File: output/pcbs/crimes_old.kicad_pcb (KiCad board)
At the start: 2 copper layers, 274.5 x 98.9 mm, 156 parts

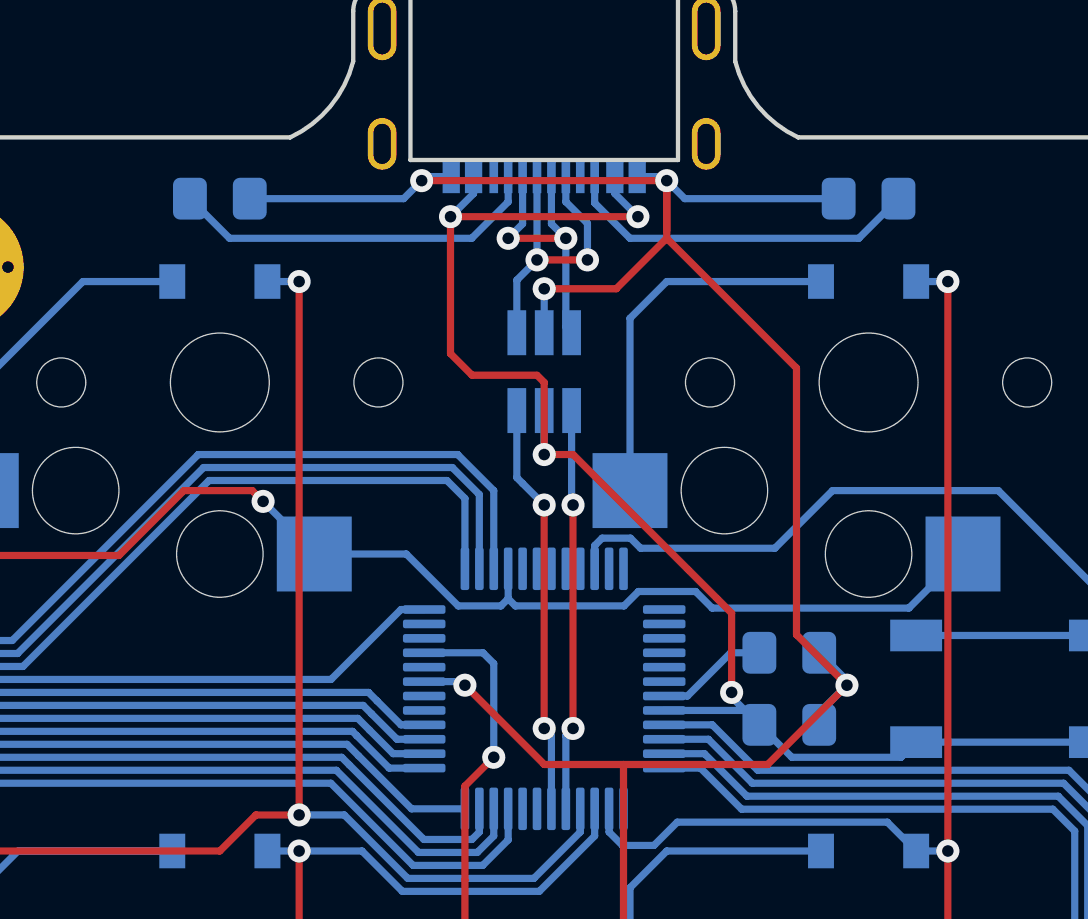
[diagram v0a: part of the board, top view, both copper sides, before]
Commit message: Fixed Pinouts.
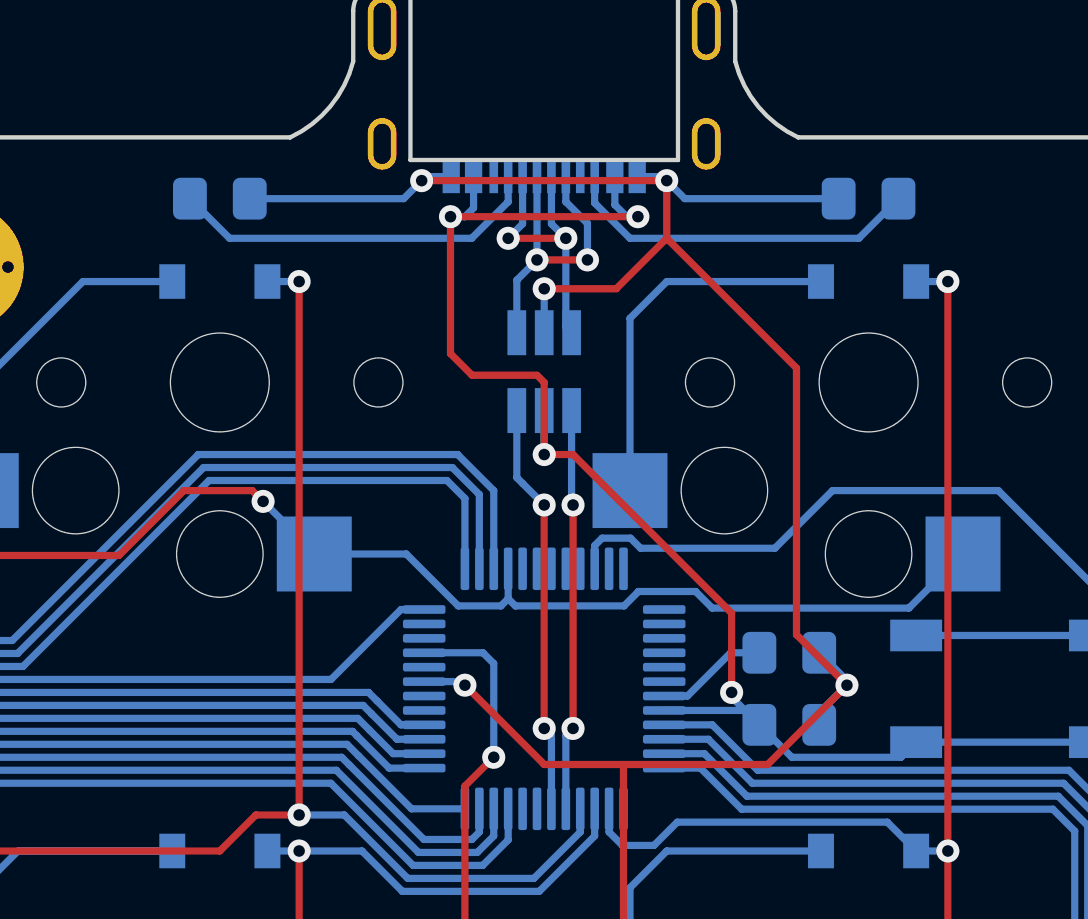
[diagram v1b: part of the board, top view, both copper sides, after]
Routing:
- net GND: track 94.6 -> 92.8 mm
- net VBUS: track 51.8 -> 52.3 mm
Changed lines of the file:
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@@
       (outputformat 1)
       (mirror false)
-      (drillshape 1)
+      (drillshape 0)
       (scaleselection 1)
-      (outputdirectory "")
+      (outputdirectory "./keyboard")
     )
   )
@@
     (fp_line (start 1 0.625) (end -1 0.625)
       (stroke (width 0.1) (type solid)) (layer "B.Fab"))
-    (pad "1" smd roundrect (at 1.0375 0) (size 1.175 1.45) (layers "B.Cu" "B.Paste" "B.Mask") (roundrect_rratio 0.212766)
+    (pad "1" smd roundrect (at 1.0375 0) (size 1.175 1.45) (layers "B.Cu" "B.Paste" "B.Mask") (roundrect_rratio 0.2127659574)
       (net 54 "CC2"))
-    (pad "2" smd roundrect (at -1.0375 0) (size 1.175 1.45) (layers "B.Cu" "B.Paste" "B.Mask") (roundrect_rratio 0.212766)
+    (pad "2" smd roundrect (at -1.0375 0) (size 1.175 1.45) (layers "B.Cu" "B.Paste" "B.Mask") (roundrect_rratio 0.2127659574)
       (net 18 "GND"))
   )
@@
     (fp_line (start 1 0.625) (end -1 0.625)
       (stroke (width 0.1) (type solid)) (layer "B.Fab"))
-    (pad "1" smd roundrect (at 1.0375 0 180) (size 1.175 1.45) (layers "B.Cu" "B.Paste" "B.Mask") (roundrect_rratio 0.212766)
+    (pad "1" smd roundrect (at 1.0375 0 180) (size 1.175 1.45) (layers "B.Cu" "B.Paste" "B.Mask") (roundrect_rratio 0.2127659574)
       (net 42 "V33"))
-    (pad "2" smd roundrect (at -1.0375 0 180) (size 1.175 1.45) (layers "B.Cu" "B.Paste" "B.Mask") (roundrect_rratio 0.212766)
+    (pad "2" smd roundrect (at -1.0375 0 180) (size 1.175 1.45) (layers "B.Cu" "B.Paste" "B.Mask") (roundrect_rratio 0.2127659574)
       (net 18 "GND"))
   )
@@
     (at 320.25 85.625)
     (attr through_hole)
-    (fp_text reference "" (at 0 0) (layer "F.SilkS")
+    (fp_text reference "" (at 0 0 180) (layer "F.SilkS")
         (effects (font (size 1.27 1.27) (thickness 0.15)))
     )
-    (fp_text value "" (at 0 0) (layer "F.SilkS")
+    (fp_text value "" (at 0 0 180) (layer "F.SilkS")
         (effects (font (size 1.27 1.27) (thickness 0.15)))
     )
-    (fp_line (start -4.64 6.66) (end -4.64 0)
-      (stroke (width 0.2) (type solid)) (layer "B.SilkS"))
-    (fp_line (start -4.64 6.66) (end 4.64 6.66)
-      (stroke (width 0.2) (type solid)) (layer "B.SilkS"))
-    (fp_line (start 0 0) (end -4.64 0)
-      (stroke (width 0.2) (type solid)) (layer "B.SilkS"))
-    (fp_line (start 0 0) (end 4.64 0)
-      (stroke (width 0.2) (type solid)) (layer "B.SilkS"))
-    (fp_line (start 4.64 6.66) (end 4.64 0)
-      (stroke (width 0.2) (type solid)) (layer "B.SilkS"))
     (pad "1" smd rect (at -3.225 7.235) (size 0.6 1.15) (layers "B.Cu" "B.Paste" "B.Mask")
       (net 18 "GND"))
@@
     (fp_line (start 1 0.625) (end -1 0.625)
       (stroke (width 0.1) (type solid)) (layer "B.Fab"))
-    (pad "1" smd roundrect (at 1.0375 0 180) (size 1.175 1.45) (layers "B.Cu" "B.Paste" "B.Mask") (roundrect_rratio 0.212766)
+    (pad "1" smd roundrect (at 1.0375 0 180) (size 1.175 1.45) (layers "B.Cu" "B.Paste" "B.Mask") (roundrect_rratio 0.2127659574)
       (net 52 "CC1"))
-    (pad "2" smd roundrect (at -1.0375 0 180) (size 1.175 1.45) (layers "B.Cu" "B.Paste" "B.Mask") (roundrect_rratio 0.212766)
+    (pad "2" smd roundrect (at -1.0375 0 180) (size 1.175 1.45) (layers "B.Cu" "B.Paste" "B.Mask") (roundrect_rratio 0.2127659574)
       (net 18 "GND"))
   )
@@
     (fp_line (start 1 0.625) (end -1 0.625)
       (stroke (width 0.1) (type solid)) (layer "B.Fab"))
-    (pad "1" smd roundrect (at 1.0375 0 180) (size 1.175 1.45) (layers "B.Cu" "B.Paste" "B.Mask") (roundrect_rratio 0.212766)
+    (pad "1" smd roundrect (at 1.0375 0 180) (size 1.175 1.45) (layers "B.Cu" "B.Paste" "B.Mask") (roundrect_rratio 0.2127659574)
       (net 41 "VBUS"))
-    (pad "2" smd roundrect (at -1.0375 0 180) (size 1.175 1.45) (layers "B.Cu" "B.Paste" "B.Mask") (roundrect_rratio 0.212766)
+    (pad "2" smd roundrect (at -1.0375 0 180) (size 1.175 1.45) (layers "B.Cu" "B.Paste" "B.Mask") (roundrect_rratio 0.2127659574)
       (net 18 "GND"))
   )
@@
   (gr_poly
     (pts
-      (xy 70.861674 151.993105)
-      (xy 70.423824 151.993105)
-      (xy 70.423824 151.664721)
-      (xy 70.861674 151.664721)
-    )
-    (stroke (width 0) (type solid)) (fill solid) (layer "B.SilkS"))
-  (gr_poly
-    (pts
       (xy 70.642987 155.550576)
       (xy 69.384006 154.278183)
@@
   (segment (start 317.5 128.625) (end 318.4 129.525) (width 0.25) (layer "B.Cu") (net 16))
   (segment (start 316.0875 109.375) (end 318.125 109.375) (width 0.25) (layer "B.Cu") (net 16))
-  (segment (start 324.5 95) (end 324.5 93) (width 0.25) (layer "F.Cu") (net 18))
   (segment (start 329 108.75) (end 329 99.5) (width 0.25) (layer "F.Cu") (net 18))
   (segment (start 322.75 96.75) (end 320.25 96.75) (width 0.25) (layer "F.Cu") (net 18))
+  (segment (start 324.5 93) (end 324.5 95) (width 0.25) (layer "F.Cu") (net 18))
   (segment (start 330.75 110.5) (end 328 113.25) (width 0.25) (layer "F.Cu") (net 18))
-  (segment (start 324.5 94.75) (end 324.5 93) (width 0.25) (layer "F.Cu") (net 18))
   (segment (start 328 113.25) (end 323 113.25) (width 0.25) (layer "F.Cu") (net 18))
   (segment (start 323 127.75) (end 323 113.25) (width 0.25) (layer "F.Cu") (net 18))
@@
   (segment (start 332.625 113) (end 333.15 112.475) (width 0.25) (layer "B.Cu") (net 41))
   (segment (start 320.25 100.975) (end 320.25 102.5) (width 0.25) (layer "B.Cu") (net 41))
+  (segment (start 323.111091 94.25) (end 323.5 94.25) (width 0.25) (layer "B.Cu") (net 41))
   (segment (start 328.8375 113) (end 332.625 113) (width 0.25) (layer "B.Cu") (net 41))
-  (segment (start 322.7 93.45) (end 323.5 94.25) (width 0.25) (layer "B.Cu") (net 41))
+  (segment (start 317.8 93.95) (end 317.5 94.25) (width 0.25) (layer "B.Cu") (net 41))
   (segment (start 326.75 110.75) (end 326.75 110.9125) (width 0.25) (layer "B.Cu") (net 41))
   (segment (start 327.2125 111.375) (end 327.7125 111.875) (width 0.25) (layer "B.Cu") (net 41))
   (segment (start 339.35 112.475) (end 333.15 112.475) (width 0.25) (layer "B.Cu") (net 41))
-  (segment (start 317.8 93.45) (end 317 94.25) (width 0.25) (layer "B.Cu") (net 41))
+  (segment (start 317.8 92.86) (end 317.8 93.95) (width 0.25) (layer "B.Cu") (net 41))
   (segment (start 324.4125 111.375) (end 327.2125 111.375) (width 0.25) (layer "B.Cu") (net 41))
   (segment (start 327.7125 111.875) (end 328.8375 113) (width 0.25) (layer "B.Cu") (net 41))
-  (segment (start 322.7 92.86) (end 322.7 93.45) (width 0.25) (layer "B.Cu") (net 41))
-  (segment (start 317.8 92.86) (end 317.8 93.45) (width 0.25) (layer "B.Cu") (net 41))
   (segment (start 327.3375 112.25) (end 327.7125 111.875) (width 0.25) (layer "B.Cu") (net 41))
+  (segment (start 322.7 92.86) (end 322.7 93.838909) (width 0.25) (layer "B.Cu") (net 41))
   (segment (start 326.75 110.9125) (end 327.7125 111.875) (width 0.25) (layer "B.Cu") (net 41))
+  (segment (start 317.5 94.25) (end 317 94.25) (width 0.25) (layer "B.Cu") (net 41))
+  (segment (start 322.7 93.838909) (end 323.111091 94.25) (width 0.25) (layer "B.Cu") (net 41))
   (segment (start 325.217764 110.875) (end 326.717764 109.375) (width 0.25) (layer "B.Cu") (net 42))
   (segment (start 324.4125 110.875) (end 325.217764 110.875) (width 0.25) (layer "B.Cu") (net 42))
